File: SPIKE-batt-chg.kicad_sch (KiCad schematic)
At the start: 9 parts, among them IC1 CN3702, IC2 CH224K, J1 USB_C_Receptacle_USB2.0

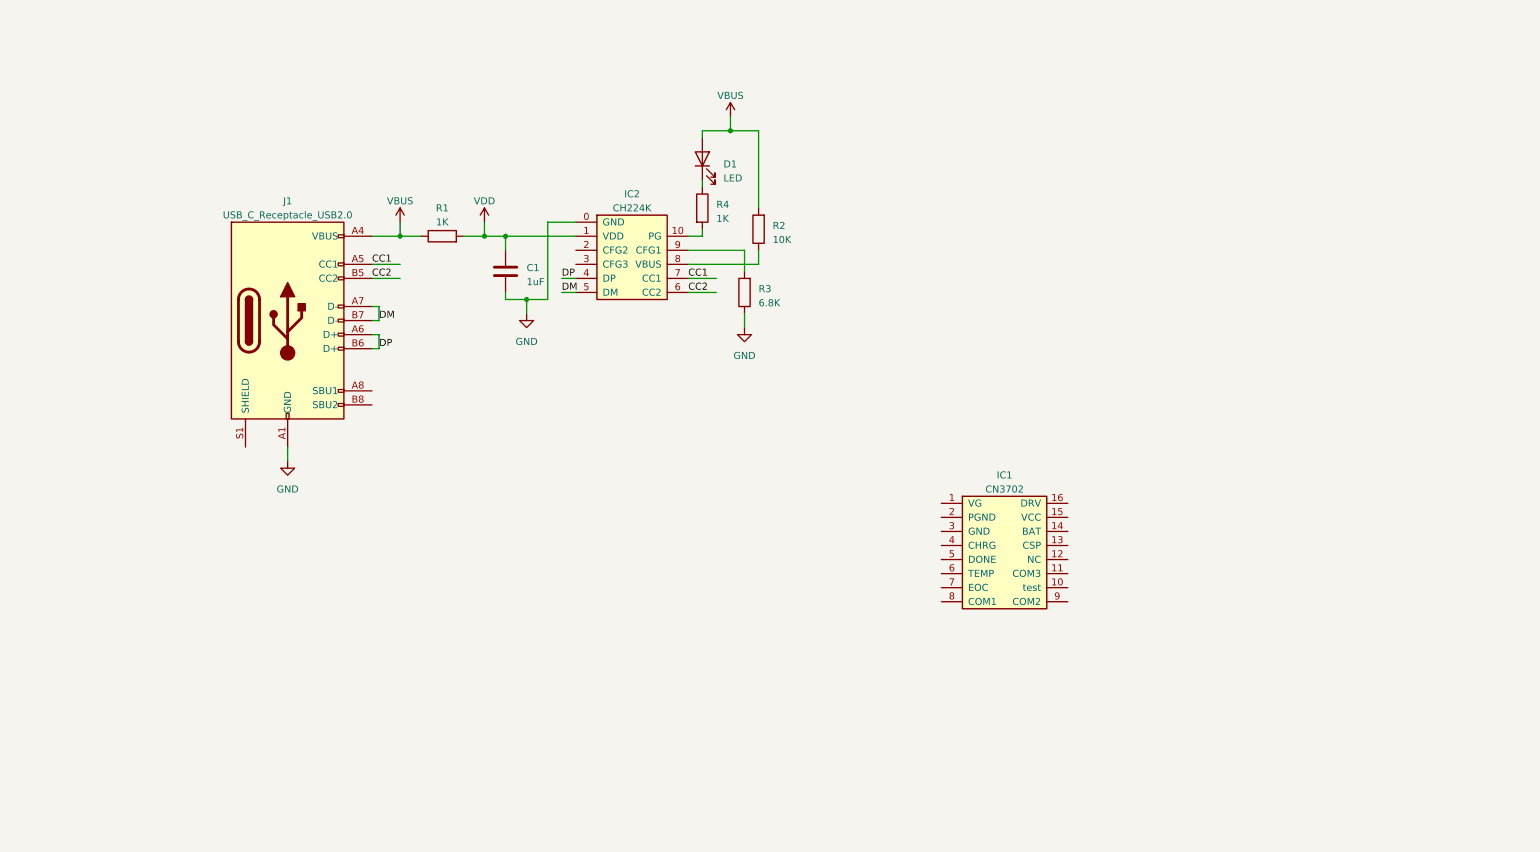
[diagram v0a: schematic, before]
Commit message: Finished CN3702 battery charging IC schematic
Added PG switch for CN3702, since the UVLO(min) is 4.6V
Yet to do: selection of schottky diode and power PMOS
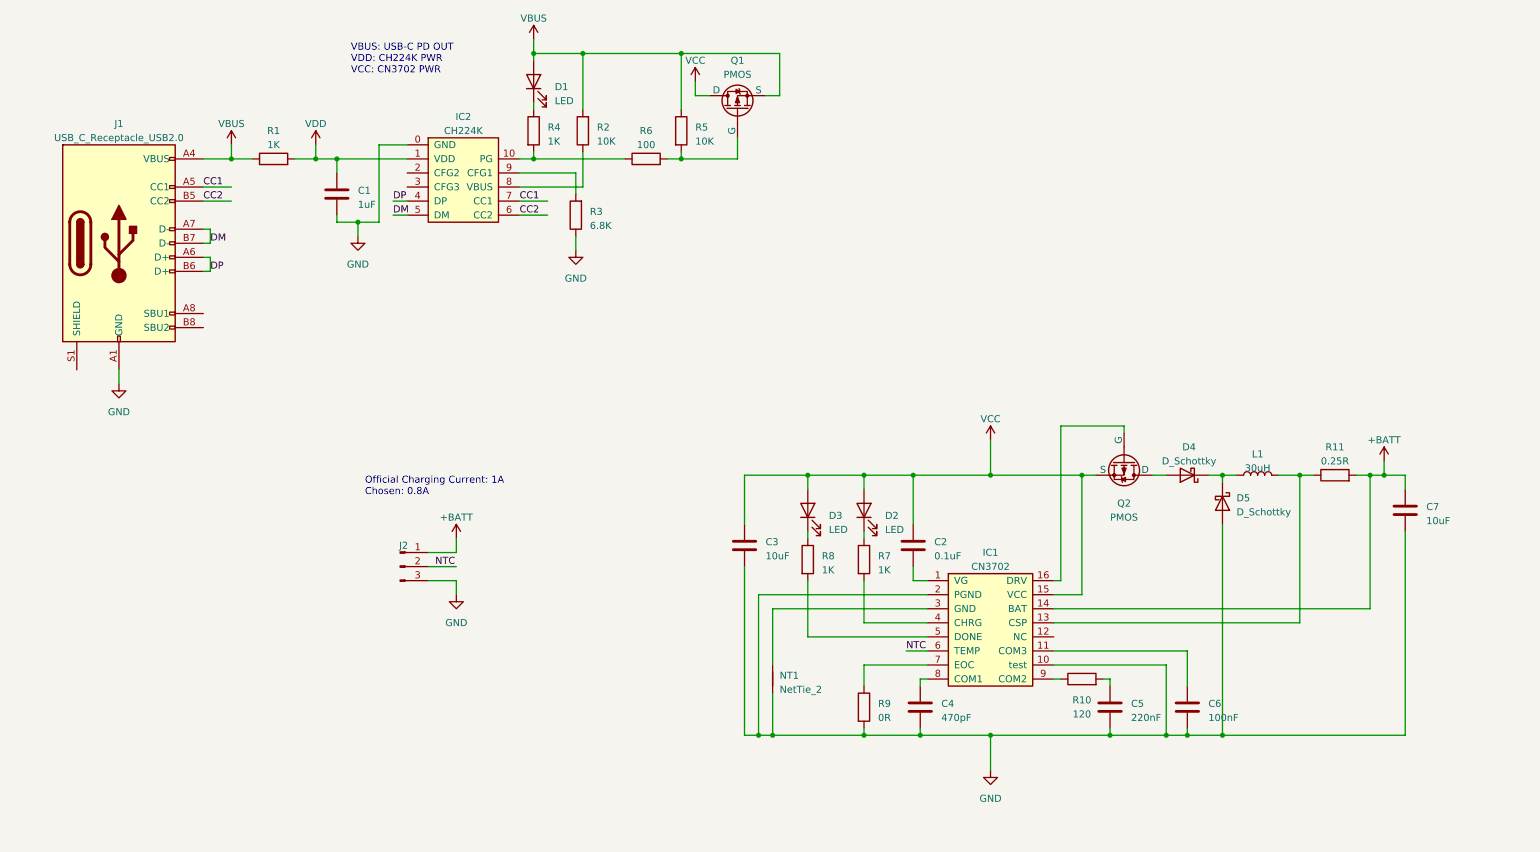
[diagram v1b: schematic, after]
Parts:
- added C2: 0.1uF, symbol Device:C
- added C3, C7: 10uF, symbol Device:C
- added C4: 470pF, symbol Device:C
- added C5: 220nF, symbol Device:C
- added C6: 100nF, symbol Device:C
- added D2, D3: LED, symbol Device:LED
- added D4, D5: D_Schottky, symbol Device:D_Schottky
- added J2: Conn_01x03_Pin, symbol Connector:Conn_01x03_Pin
- added L1: 30uH, symbol Device:L
- added NT1: NetTie_2, symbol Device:NetTie_2
- added Q1, Q2: PMOS, symbol Simulation_SPICE:PMOS
- added R10: 120, symbol Device:R
- added R11: 0.25R, symbol Device:R
- added R5: 10K, symbol Device:R
- added R6: 100, symbol Device:R
- added R7, R8: 1K, symbol Device:R
- added R9: 0R, symbol Device:R
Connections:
- net GND: now also IC1.10 (test), IC1.2 (PGND), C3.2, C4.2, C5.2, C6.2, C7.2, D5.2 (A), J2.3 (Pin_3), NT1.1, R9.2
- net VBUS: now also Q1.3 (S), R5.1
- net at IC2.10 (PG), R4.2: now also R6.1
- net at IC1.1 (VG): now also C2.2
- net at IC1.11 (COM3): now also C6.1
- net at IC1.13 (CSP): now also L1.2, R11.1
- net +BATT: now reaches IC1.14 (BAT)
- net +BATT: now also C7.1, J2.1 (Pin_1), R11.2
- net VCC: now reaches IC1.15 (VCC)
- net VCC: now also C2.1, C3.1, D2.2 (A), D3.2 (A), Q1.1 (D), Q2.3 (S)
- net at IC1.16 (DRV): now also Q2.2 (G)
- net at IC1.3 (GND): now also NT1.2
- net at IC1.4 (CHRG): now also R7.2
- net at IC1.5 (DONE): now also R8.2
- net NTC: now reaches IC1.6 (TEMP)
- net NTC: now also J2.2 (Pin_2)
- net at IC1.7 (EOC): now also R9.1
- net at IC1.8 (COM1): now also C4.1
- net at IC1.9 (COM2): now also R10.1
- new net: D2.1 (K), R7.1
- new net: D3.1 (K), R8.1
- new net: Q1.2 (G), R5.2, R6.2
- new net: D4.1 (K), D5.1 (K), L1.1
- new net: D4.2 (A), Q2.1 (D)
- new net: C5.1, R10.2
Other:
- note added: "Official Charging Current: 1A Chosen: 0.8A"
- note added: "VBUS: USB-C PD OUT VDD: CH224K PWR VCC: CN3702 PWR"
- moved on the sheet: C1, D1, IC1, IC2, J1, R1, R2, R3, R4

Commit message: Split charger into hierarchical sheets 4 charging circuits will be on the board Added jumper for PD voltage selection (9V or 20V) Added SPDT switch to TEMP pin to turn on/off charger
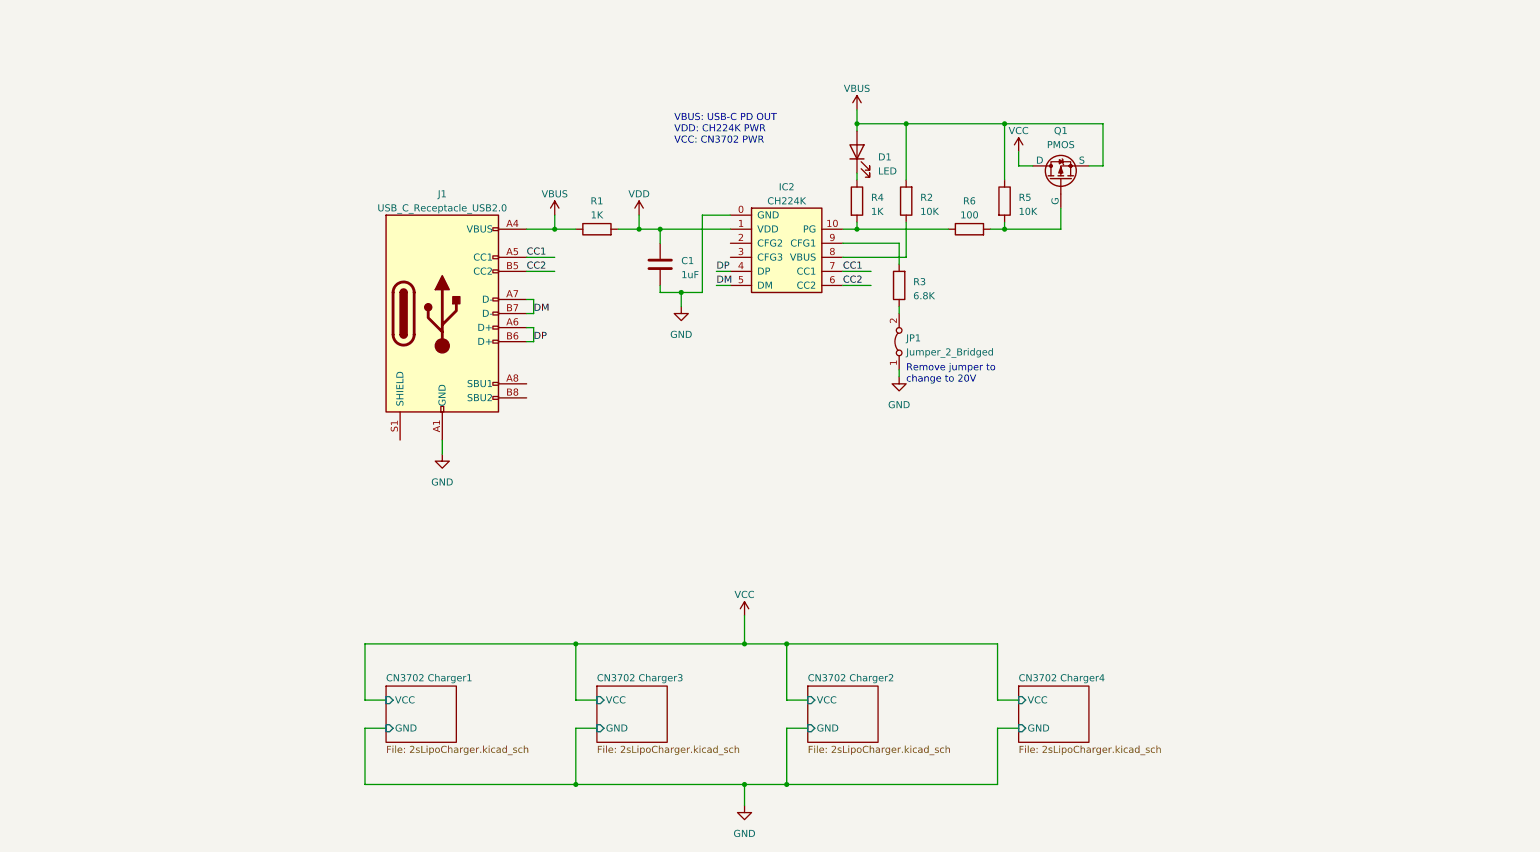
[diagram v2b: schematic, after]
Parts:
- removed C2: 0.1uF, symbol Device:C
- removed C3, C7: 10uF, symbol Device:C
- removed C4: 470pF, symbol Device:C
- removed C5: 220nF, symbol Device:C
- removed C6: 100nF, symbol Device:C
- removed D2, D3: LED, symbol Device:LED
- removed D4, D5: D_Schottky, symbol Device:D_Schottky
- removed IC1: CN3702, symbol Connector_Generic:Conn_02x08_Counter_Clockwise
- removed J2: Conn_01x03_Pin, symbol Connector:Conn_01x03_Pin
- removed L1: 30uH, symbol Device:L
- removed NT1: NetTie_2, symbol Device:NetTie_2
- removed Q2: PMOS, symbol Simulation_SPICE:PMOS
- removed R10: 120, symbol Device:R
- removed R11: 0.25R, symbol Device:R
- removed R7, R8: 1K, symbol Device:R
- removed R9: 0R, symbol Device:R
- added JP1: Jumper_2_Bridged, TestPoint:TestPoint_2Pads_Pitch2.54mm_Drill0.8mm, symbol Jumper:Jumper_2_Bridged
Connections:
- net GND: now also JP1.1 (A); no longer R3.1
- new net: JP1.2 (B), R3.1
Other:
- added sheet CN3702 Charger1 (2sLipoCharger.kicad_sch)
- added sheet CN3702 Charger2 (2sLipoCharger.kicad_sch)
- added sheet CN3702 Charger3 (2sLipoCharger.kicad_sch)
- added sheet CN3702 Charger4 (2sLipoCharger.kicad_sch)
- note added: "Remove jumper to change to 20V"
- note removed: "Official Charging Current: 1A Chosen: 0.8A"
- moved on the sheet: C1, D1, IC2, J1, Q1, R1, R2, R3, R4, R5, R6

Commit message: Finished Schematic
- Cleaned up page 1
- Only 3 chargers / board now
- LED no longer activated by PG, connected to VCC after the P-MOSFET instead
- Added DC barrel jack for daisy chaining (using M-M 30cm cable)

- Added jumper to enable fast charge
- Selected inductor, diode, P-MOSFET, current sense resistor
- Changed slide switch to 90 degree
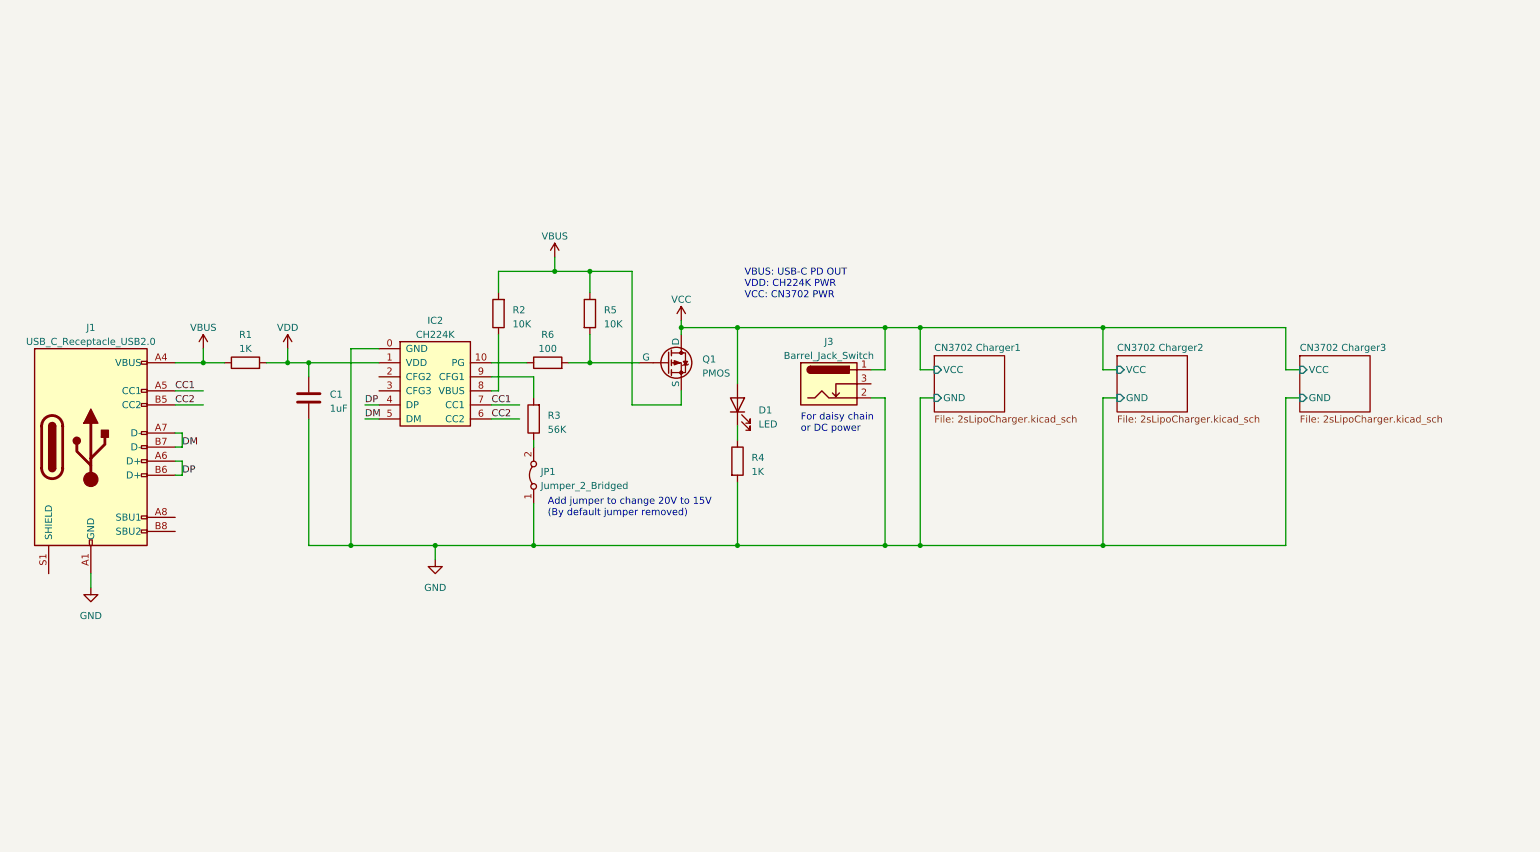
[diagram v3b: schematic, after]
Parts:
- added J3: Barrel_Jack_Switch, symbol Connector:Barrel_Jack_Switch
- R3: value 6.8K -> 56K
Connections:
- net GND: now also R4.2, J3.2
- net VBUS: no longer D1.2 (A)
- net VCC: now also D1.2 (A), J3.1
- net at IC2.10 (PG), R6.1: no longer R4.2
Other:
- removed sheet CN3702 Charger4
- note added: "Add jumper to change 20V to 15V (By default jumper removed)"
- note added: "For daisy chain or DC power"
- note removed: "Remove jumper to change to 20V"
- moved on the sheet: C1, D1, IC2, J1, JP1, Q1, R1, R2, R3, R4, R5, R6

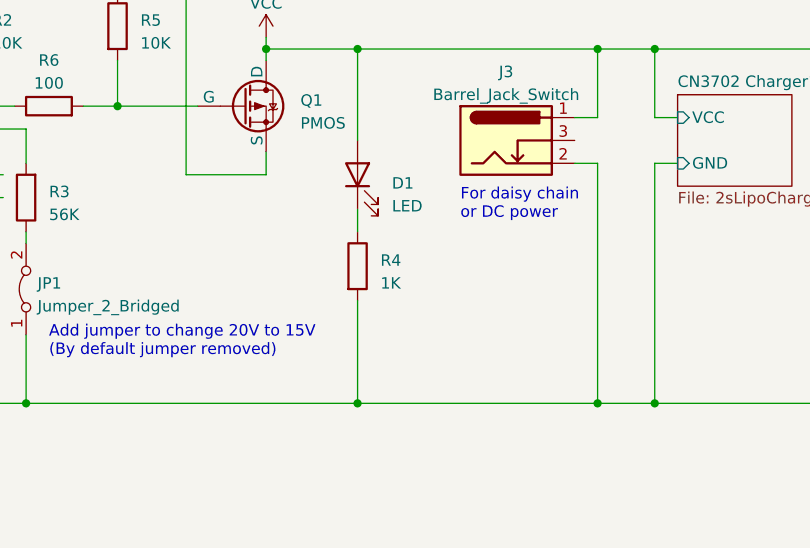
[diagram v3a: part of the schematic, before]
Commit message: Footprint assignment partially done
- incomplete: minor edit of footprints, locking pin header footprints
- changed LEDs to side facing, changed PG LED resistor to 4.7k since
  will be going through 20V
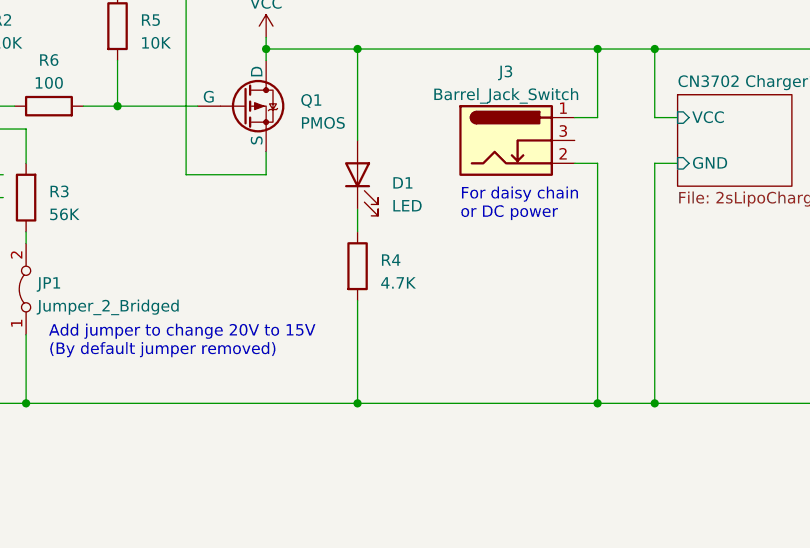
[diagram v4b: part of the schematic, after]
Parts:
- C1: footprint (none) -> Capacitor_SMD:C_0603_1608Metric
- D1: footprint (none) -> LED_SMD:LED_0603_1608Metric; JLCPCB Part # (none) -> C965863; Part (none) -> XL-1606UGC
- Q1: footprint (none) -> Package_TO_SOT_SMD:SOT-23
- R1, R2, R3, R5, R6: footprint (none) -> Resistor_SMD:R_0603_1608Metric
- R4: value 1K -> 4.7K; footprint (none) -> Resistor_SMD:R_0603_1608Metric
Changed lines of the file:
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@@
       (effects (font (size 1.27 1.27)) (justify left))
     )
-    (property "Footprint" "" (at 70.8152 91.44 0)
+    (property "Footprint" "Capacitor_SMD:C_0603_1608Metric" (at 70.8152 91.44 0)
       (effects (font (size 1.27 1.27)) hide)
     )
@@
       (effects (font (size 1.27 1.27)) (justify left))
     )
-    (property "Value" "1K" (at 149.86 100.965 0)
-      (effects (font (size 1.27 1.27)) (justify left))
-    )
-    (property "Footprint" "" (at 145.542 99.06 90)
+    (property "Value" "4.7K" (at 149.86 100.965 0)
+      (effects (font (size 1.27 1.27)) (justify left))
+    )
+    (property "Footprint" "Resistor_SMD:R_0603_1608Metric" (at 145.542 99.06 90)
       (effects (font (size 1.27 1.27)) hide)
     )
@@
       (effects (font (size 1.27 1.27)) (justify right))
     )
-    (property "Footprint" "" (at 147.32 88.9 0)
+    (property "Footprint" "LED_SMD:LED_0603_1608Metric" (at 147.32 88.9 0)
       (effects (font (size 1.27 1.27)) hide)
     )
@@
       (effects (font (size 1.27 1.27)) hide)
     )
+    (property "Part" "XL-1606UGC" (at 147.32 88.9 90)
+      (effects (font (size 1.27 1.27)) hide)
+    )
+    (property "JLCPCB Part #" "C965863" (at 147.32 88.9 90)
+      (effects (font (size 1.27 1.27)) hide)
+    )
     (pin "1")
     (pin "2")
@@
       (effects (font (size 1.27 1.27)))
     )
-    (property "Footprint" "" (at 113.03 83.058 90)
+    (property "Footprint" "Resistor_SMD:R_0603_1608Metric" (at 113.03 83.058 90)
       (effects (font (size 1.27 1.27)) hide)
     )
@@
       (effects (font (size 1.27 1.27)) (justify left))
     )
-    (property "Footprint" "" (at 118.872 72.39 90)
+    (property "Footprint" "Resistor_SMD:R_0603_1608Metric" (at 118.872 72.39 90)
       (effects (font (size 1.27 1.27)) hide)
     )
@@
       (effects (font (size 1.27 1.27)))
     )
-    (property "Footprint" "" (at 58.42 83.058 90)
+    (property "Footprint" "Resistor_SMD:R_0603_1608Metric" (at 58.42 83.058 90)
       (effects (font (size 1.27 1.27)) hide)
     )
@@
       (effects (font (size 1.27 1.27)) (justify right))
     )
-    (property "Footprint" "" (at 105.918 72.39 90)
+    (property "Footprint" "Resistor_SMD:R_0603_1608Metric" (at 105.918 72.39 90)
       (effects (font (size 1.27 1.27)) hide)
     )
@@
       (effects (font (size 1.27 1.27)) (justify left))
     )
-    (property "Footprint" "" (at 139.7 78.74 0)
+    (property "Footprint" "Package_TO_SOT_SMD:SOT-23" (at 139.7 78.74 0)
       (effects (font (size 1.27 1.27)) hide)
     )
@@
       (effects (font (size 1.27 1.27)) (justify right))
     )
-    (property "Footprint" "" (at 112.268 91.44 90)
-      (effects (font (size 1.27 1.27)) hide)
-    )
+    (property "Footprint" "Resistor_SMD:R_0603_1608Metric" (at 112.268 91.44 90)
+      (effects (font (size 1.27 1.27)) hide)
+    )
